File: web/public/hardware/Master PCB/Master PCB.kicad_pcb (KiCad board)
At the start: 2 copper layers, 100 x 100 mm, 100 parts, among them J1 Rows 0-15, J10 LDR2, J11 LDR3, J12 LDR4, J13 SWD Conn, J14 LED Conn, J15 OLED1, J16 OLED2, J17 Relay Conn, J2 Cols 0-21, J3 Cols 22-31, J4 5V_IN, J5 LED1, J6 LED2, J7 LED3, J8 LED4, J9 LDR1, Q1 2N7000, Q2 2N7000, Q3 2N7000, Q4 2N7000, SW1 nRST, SW2 Menu Encoder, U1 STM32U585VITx, U2 M95P32-IXMNT, U3 TLV62568DBV, U4 LM339, U5 MAX7375AXR805, U6 USBLC6-4SC6, U7 USBLC6-2SC6, U8 USBLC6-2SC6

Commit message: Stitch ground plane under STM32
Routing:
- net GND: track 93.5 -> 96.3 mm, vias 30 -> 32
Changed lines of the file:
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@@
   (segment (start 134.0375 98.2625) (end 134 98.3) (width 0.25) (layer "F.Cu") (net 2))
   (segment (start 129.75 97.0625) (end 129.75 98.35) (width 0.25) (layer "F.Cu") (net 2))
+  (segment (start 150.7 98.9) (end 152.7 98.9) (width 0.25) (layer "F.Cu") (net 2))
   (segment (start 145.361056 94.051741) (end 146.831644 94.051741) (width 0.25) (layer "F.Cu") (net 2))
   (segment (start 168.095 106.295) (end 168 106.2) (width 0.25) (layer "F.Cu") (net 2))
@@
   (segment (start 111.7 102) (end 111.7 103.6) (width 0.25) (layer "F.Cu") (net 2))
   (segment (start 138.2 98.3) (end 137.9 98.3) (width 0.25) (layer "F.Cu") (net 2))
+  (segment (start 150.1 98.3) (end 150.7 98.9) (width 0.25) (layer "F.Cu") (net 2))
   (segment (start 126.1 74.6625) (end 126.1 74.278249) (width 0.25) (layer "F.Cu") (net 2))
   (segment (start 111.7 86) (end 111.7 87.6) (width 0.25) (layer "F.Cu") (net 2))
@@
   (via (at 115.5 147.7) (size 0.8) (drill 0.4) (layers "F.Cu" "B.Cu") (net 2))
   (via (at 168 106.2) (size 0.8) (drill 0.4) (layers "F.Cu" "B.Cu") (net 2))
+  (via (at 152.7 98.9) (size 0.8) (drill 0.4) (layers "F.Cu" "B.Cu") (free) (net 2))
   (via (at 185.1 105.5) (size 0.8) (drill 0.4) (layers "F.Cu" "B.Cu") (net 2))
   (via (at 124.6 73.1) (size 0.8) (drill 0.4) (layers "F.Cu" "B.Cu") (net 2))
@@
   (via (at 144.5 105.9) (size 0.8) (drill 0.4) (layers "F.Cu" "B.Cu") (net 2))
   (via (at 171.6 109.6) (size 0.8) (drill 0.4) (layers "F.Cu" "B.Cu") (net 2))
+  (via (at 150.1 98.3) (size 0.8) (drill 0.4) (layers "F.Cu" "B.Cu") (free) (net 2))
   (via (at 155.9 110) (size 0.8) (drill 0.4) (layers "F.Cu" "B.Cu") (net 2))
   (via (at 142.9 109.5) (size 0.8) (drill 0.4) (layers "F.Cu" "B.Cu") (net 2))
@@
   (segment (start 127.05 74.278249) (end 127.05 74.6625) (width 0.25) (layer "F.Cu") (net 9))
   (segment (start 116 66.8) (end 116 69) (width 0.25) (layer "F.Cu") (net 9))
-  (segment (start 142.225 93.9) (end 134.21948 93.9) (width 0.25) (layer "F.Cu") (net 10))
+  (segment (start 140.4 94) (end 140.3 93.9) (width 0.25) (layer "F.Cu") (net 10))
+  (segment (start 140.3 93.9) (end 134.21948 93.9) (width 0.25) (layer "F.Cu") (net 10))
+  (segment (start 142.325 94) (end 140.4 94) (width 0.25) (layer "F.Cu") (net 10))
   (segment (start 133.473344 56.173344) (end 133.3 56) (width 0.25) (layer "F.Cu") (net 10))
-  (segment (start 142.325 94) (end 142.225 93.9) (width 0.25) (layer "F.Cu") (net 10))
   (segment (start 134.21948 93.9) (end 133.473344 93.153864) (width 0.25) (layer "F.Cu") (net 10))
   (segment (start 133.473344 93.153864) (end 133.473344 56.173344) (width 0.25) (layer "F.Cu") (net 10))

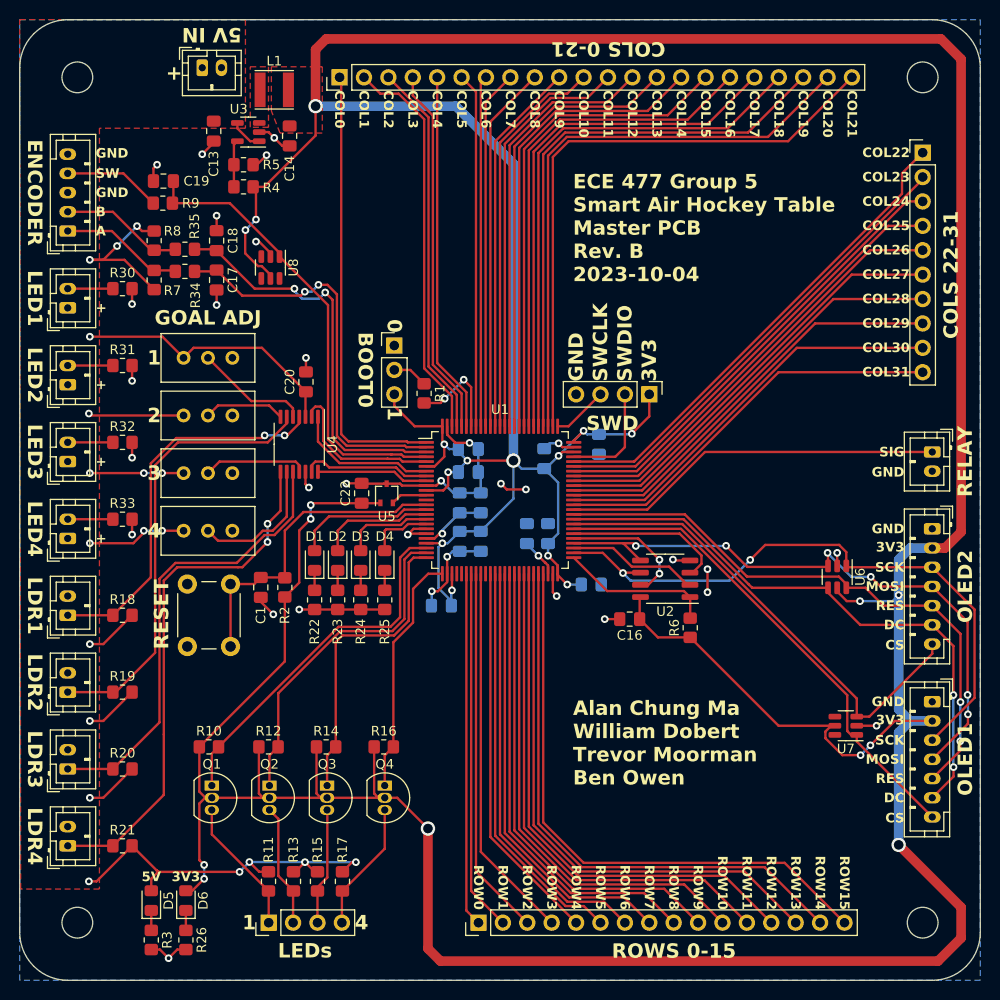
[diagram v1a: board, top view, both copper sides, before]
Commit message: Miscellaneous trace cleanup
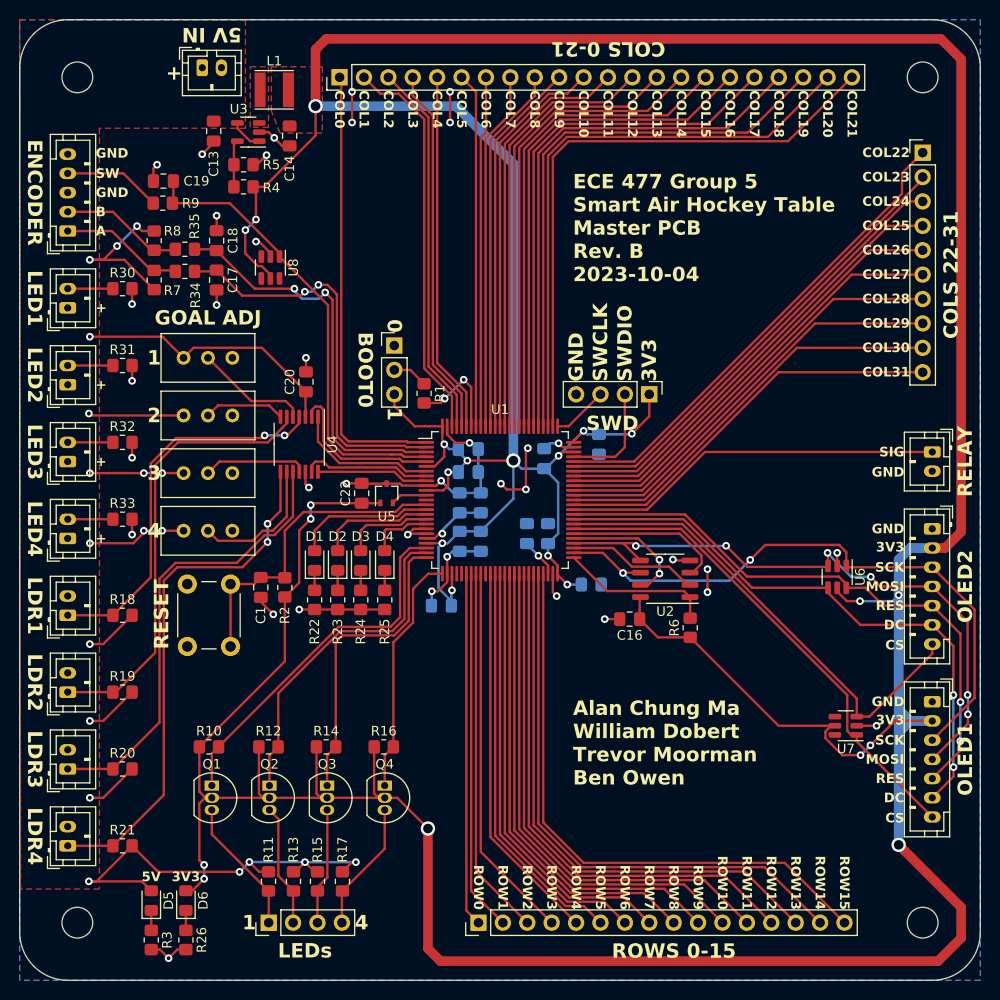
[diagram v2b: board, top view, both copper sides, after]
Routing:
- net GND: track 96.3 -> 107.1 mm, vias 32 -> 37
- net +5V: track 136.1 -> 140.6 mm
- net +3V3: track 562.1 -> 564.5 mm
- net /COL6: track 35.8 -> 36.5 mm
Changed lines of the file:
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@@
   (segment (start 150.7 98.9) (end 152.7 98.9) (width 0.25) (layer "F.Cu") (net 2))
   (segment (start 145.361056 94.051741) (end 146.831644 94.051741) (width 0.25) (layer "F.Cu") (net 2))
+  (segment (start 134.6 57.5) (end 134.6 60.7) (width 0.25) (layer "F.Cu") (net 2))
   (segment (start 168.095 106.295) (end 168 106.2) (width 0.25) (layer "F.Cu") (net 2))
   (segment (start 124.3 65.1) (end 124.7 65.1) (width 0.25) (layer "F.Cu") (net 2))
+  (segment (start 152.7 98.9) (end 152.7 94.8) (width 0.25) (layer "F.Cu") (net 2))
   (segment (start 111.7 94) (end 111.7 95.6) (width 0.25) (layer "F.Cu") (net 2))
   (segment (start 142.325 98.5) (end 143.3755 98.5) (width 0.25) (layer "F.Cu") (net 2))
   (segment (start 141 103) (end 140.4 103.6) (width 0.25) (layer "F.Cu") (net 2))
+  (segment (start 152.7 94.8) (end 152.9 94.6) (width 0.25) (layer "F.Cu") (net 2))
+  (segment (start 144.8 57.5) (end 144.8 60.7) (width 0.25) (layer "F.Cu") (net 2))
   (segment (start 135.5 111.4) (end 133.1 111.4) (width 0.25) (layer "F.Cu") (net 2))
   (segment (start 120.2 62.6375) (end 120.2 62.8) (width 0.25) (layer "F.Cu") (net 2))
@@
   (via (at 130.1 98.7) (size 0.8) (drill 0.4) (layers "F.Cu" "B.Cu") (net 2))
   (via (at 160.9 112.4) (size 0.8) (drill 0.4) (layers "F.Cu" "B.Cu") (net 2))
+  (via (at 134.6 57.5) (size 0.8) (drill 0.4) (layers "F.Cu" "B.Cu") (free) (net 2))
   (via (at 126.4 111.9) (size 0.8) (drill 0.4) (layers "F.Cu" "B.Cu") (net 2))
   (via (at 111.7 87.6) (size 0.8) (drill 0.4) (layers "F.Cu" "B.Cu") (net 2))
@@
   (via (at 115.5 147.7) (size 0.8) (drill 0.4) (layers "F.Cu" "B.Cu") (net 2))
   (via (at 168 106.2) (size 0.8) (drill 0.4) (layers "F.Cu" "B.Cu") (net 2))
+  (via (at 152.9 94.6) (size 0.8) (drill 0.4) (layers "F.Cu" "B.Cu") (net 2))
   (via (at 152.7 98.9) (size 0.8) (drill 0.4) (layers "F.Cu" "B.Cu") (free) (net 2))
   (via (at 185.1 105.5) (size 0.8) (drill 0.4) (layers "F.Cu" "B.Cu") (net 2))
@@
   (via (at 150.1 98.3) (size 0.8) (drill 0.4) (layers "F.Cu" "B.Cu") (free) (net 2))
   (via (at 155.9 110) (size 0.8) (drill 0.4) (layers "F.Cu" "B.Cu") (net 2))
+  (via (at 144.8 57.5) (size 0.8) (drill 0.4) (layers "F.Cu" "B.Cu") (free) (net 2))
   (via (at 142.9 109.5) (size 0.8) (drill 0.4) (layers "F.Cu" "B.Cu") (net 2))
+  (via (at 144.8 60.7) (size 0.8) (drill 0.4) (layers "F.Cu" "B.Cu") (free) (net 2))
+  (via (at 134.6 60.7) (size 0.8) (drill 0.4) (layers "F.Cu" "B.Cu") (free) (net 2))
   (via (at 171.6 107.2) (size 0.8) (drill 0.4) (layers "F.Cu" "B.Cu") (net 2))
   (via (at 111.7 103.6) (size 0.8) (drill 0.4) (layers "F.Cu" "B.Cu") (net 2))
@@
   (segment (start 192.7 105) (end 191.5 106.2) (width 1) (layer "B.Cu") (net 4))
   (segment (start 191.5 121.8) (end 192.7 123) (width 1) (layer "B.Cu") (net 4))
+  (segment (start 191.5 121.8) (end 191.5 124.2) (width 1) (layer "B.Cu") (net 4))
   (segment (start 130.3 100.5255) (end 130.3 101.9745) (width 0.25) (layer "B.Cu") (net 4))
   (segment (start 148 103.2625) (end 145.8 103.2625) (width 0.25) (layer "B.Cu") (net 4))
@@
   (segment (start 134.6 137.7) (end 133.6 138.7) (width 0.25) (layer "F.Cu") (net 6))
   (segment (start 114 78.1) (end 110.9 75) (width 0.25) (layer "F.Cu") (net 6))
-  (segment (start 111.7 136) (end 108 139.7) (width 0.25) (layer "F.Cu") (net 6))
-  (segment (start 113.7 139.424598) (end 114.312299 138.812299) (width 0.25) (layer "F.Cu") (net 6))
+  (segment (start 113.7 140.675) (end 112.725 139.7) (width 0.25) (layer "F.Cu") (net 6))
   (segment (start 107.4 91.2) (end 107.2 91) (width 0.25) (layer "F.Cu") (net 6))
   (segment (start 117.06 103.2) (end 114.8245 103.2) (width 0.25) (layer "F.Cu") (net 6))
-  (segment (start 113.7 140.675) (end 113.7 139.424598) (width 0.25) (layer "F.Cu") (net 6))
   (segment (start 111.825305 104.5) (end 107.3 104.5) (width 0.25) (layer "F.Cu") (net 6))
   (segment (start 112.724598 72) (end 112.212299 71.487701) (width 0.25) (layer "F.Cu") (net 6))
-  (segment (start 114.312299 138.812299) (end 114.312299 138.612299) (width 0.25) (layer "F.Cu") (net 6))
+  (segment (start 112.725 139.7) (end 107.2 139.7) (width 0.25) (layer "F.Cu") (net 6))
   (segment (start 135 137.7) (end 134.6 137.7) (width 0.25) (layer "F.Cu") (net 6))
   (segment (start 117.06 91.2) (end 107.4 91.2) (width 0.25) (layer "F.Cu") (net 6))
@@
   (segment (start 128.5 138.7) (end 128.7 138.7) (width 0.25) (layer "F.Cu") (net 6))
   (segment (start 110.137701 73.562299) (end 108.7 75) (width 0.25) (layer "F.Cu") (net 6))
-  (segment (start 108 139.7) (end 107.2 139.7) (width 0.25) (layer "F.Cu") (net 6))
   (segment (start 112.9255 97.2) (end 107.3 97.2) (width 0.25) (layer "F.Cu") (net 6))
   (segment (start 114.312299 138.612299) (end 114.25 138.55) (width 0.25) (layer "F.Cu") (net 6))
@@
   (segment (start 129.75 91.3375) (end 129.75 88.7875) (width 0.25) (layer "F.Cu") (net 6))
   (segment (start 125.2175 84.155) (end 118.105 84.155) (width 0.25) (layer "F.Cu") (net 6))
-  (segment (start 114.312299 138.812299) (end 114.412299 138.712299) (width 0.25) (layer "F.Cu") (net 6))
+  (segment (start 107.2 139.7) (end 108 139.7) (width 0.25) (layer "F.Cu") (net 6))
   (segment (start 114.25 138.55) (end 111.7 136) (width 0.25) (layer "F.Cu") (net 6))
   (segment (start 125.9 138.7) (end 124.924598 138.7) (width 0.25) (layer "F.Cu") (net 6))
   (segment (start 112.9255 103.2) (end 112.9255 103.399805) (width 0.25) (layer "F.Cu") (net 6))
+  (segment (start 108 139.7) (end 111.7 136) (width 0.25) (layer "F.Cu") (net 6))
   (segment (start 114 72) (end 112.724598 72) (width 0.25) (layer "F.Cu") (net 6))
   (via (at 114.8245 103.2) (size 0.8) (drill 0.4) (layers "F.Cu" "B.Cu") (net 6))
@@
   (segment (start 147.5 92.325) (end 147.5 57.5) (width 0.25) (layer "F.Cu") (net 15))
   (segment (start 147.5 57.5) (end 146 56) (width 0.25) (layer "F.Cu") (net 15))
-  (segment (start 148 56.54) (end 148 92.325) (width 0.25) (layer "F.Cu") (net 16))
-  (segment (start 148.5 58.58) (end 151.08 56) (width 0.25) (layer "F.Cu") (net 17))
-  (segment (start 148.5 92.325) (end 148.5 58.58) (width 0.25) (layer "F.Cu") (net 17))
-  (segment (start 149 92.325) (end 149 60.62) (width 0.25) (layer "F.Cu") (net 18))
-  (segment (start 149 60.62) (end 153.62 56) (width 0.25) (layer "F.Cu") (net 18))
+  (segment (start 148 62.250812) (end 148.54 61.710812) (width 0.25) (layer "F.Cu") (net 16))
+  (segment (start 148.54 61.710812) (end 148.54 56) (width 0.25) (layer "F.Cu") (net 16))
+  (segment (start 148 92.325) (end 148 62.250812) (width 0.25) (layer "F.Cu") (net 16))
+  (segment (start 148.5 62.387208) (end 151.08 59.807208) (width 0.25) (layer "F.Cu") (net 17))
+  (segment (start 151.08 59.807208) (end 151.08 56) (width 0.25) (layer "F.Cu") (net 17))
+  (segment (start 148.5 92.325) (end 148.5 62.387208) (width 0.25) (layer "F.Cu") (net 17))
+  (segment (start 149 92.325) (end 149 62.523604) (width 0.25) (layer "F.Cu") (net 18))
+  (segment (start 149 62.523604) (end 153.62 57.903604) (width 0.25) (layer "F.Cu") (net 18))
+  (segment (start 153.62 57.903604) (end 153.62 56) (width 0.25) (layer "F.Cu") (net 18))
   (segment (start 149.5 92.325) (end 149.5 62.66) (width 0.25) (layer "F.Cu") (net 19))
   (segment (start 149.5 62.66) (end 156.16 56) (width 0.25) (layer "F.Cu") (net 19))

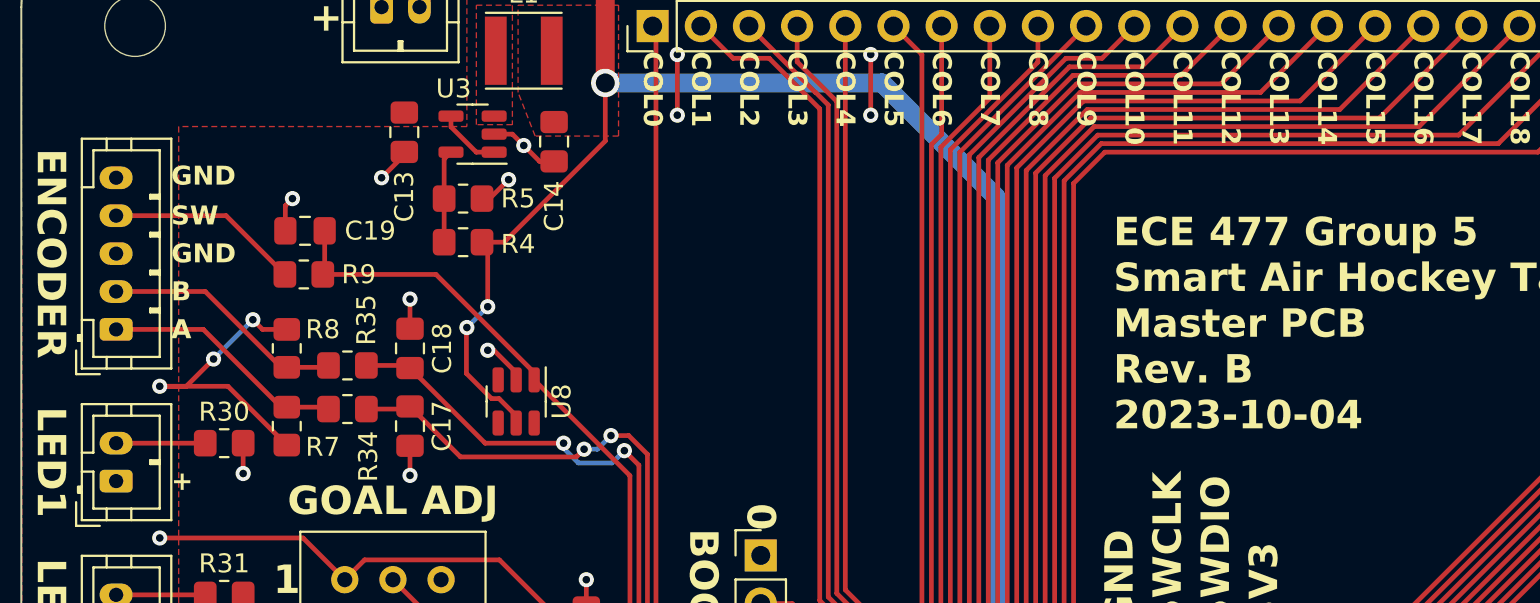
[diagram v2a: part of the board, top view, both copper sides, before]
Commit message: Fix encoder schematic and miscellaneous cleanup (new date, etc.)
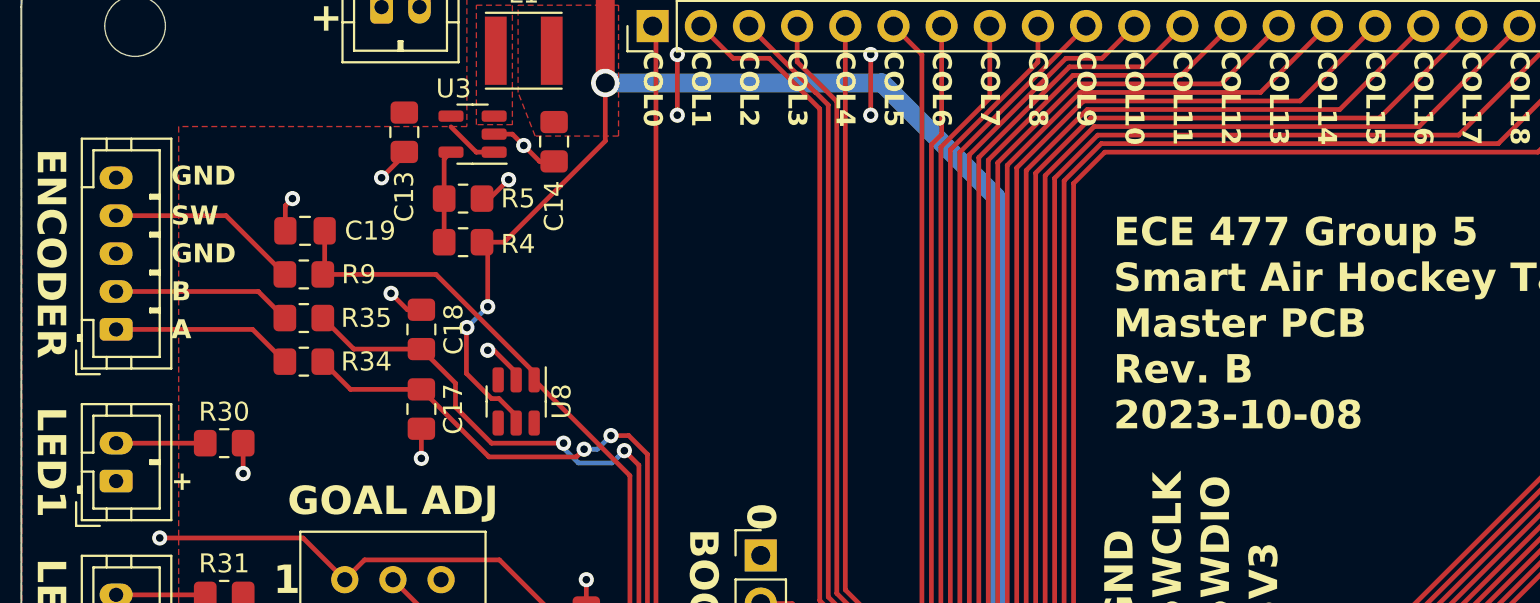
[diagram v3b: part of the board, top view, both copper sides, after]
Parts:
- removed R7, R8: 10K, Resistor_SMD:R_0805_2012Metric_Pad1.20x1.40mm_HandSolder
- moved R34 3.40 mm to (114.9, 73.7)
- moved R35 3.40 mm to (114.9, 71.4)
- moved C18 1.17 mm to (121.1, 72.0)
- moved C17 1.08 mm to (121.1, 76.2)
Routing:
- net +5V: track 140.6 -> 123.7 mm, vias 19 -> 16
- net /Menu Encoder/ENCODER_B: track 42.0 -> 46.0 mm
- net Net-(SW2-A): track 13.4 -> 9.60 mm
- net Net-(SW2-B): track 13.2 -> 9.48 mm
- net /Menu Encoder/ENCODER_A: track 41.4 -> 44.6 mm
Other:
- board text added: "ECE 477 Group 5 Smart Air Hockey Table Master PCB Rev. B 2023-10-08"
- board text removed: "ECE 477 Group 5 Smart Air Hockey Table Master PCB Rev. B 2023-10-04"

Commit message: More misc. cleanup and generate updated production files
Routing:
- net +5V: track 123.7 -> 124.2 mm
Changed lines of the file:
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@@
   (segment (start 131 138.7) (end 130.7 138.7) (width 0.25) (layer "F.Cu") (net 6))
   (segment (start 129.8 88.7375) (end 125.2175 84.155) (width 0.25) (layer "F.Cu") (net 6))
+  (segment (start 122.6625 61.315749) (end 122.6625 60.75) (width 0.25) (layer "F.Cu") (net 6))
   (segment (start 114.412299 138.712299) (end 114.25 138.55) (width 0.25) (layer "F.Cu") (net 6))
   (segment (start 128.5 138.7) (end 128.7 138.7) (width 0.25) (layer "F.Cu") (net 6))
